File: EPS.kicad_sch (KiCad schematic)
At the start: 10 parts, among them J1 G125-MH10805M4-1AD1ADP, J2 PH1RA-02-UA, J3 WJ126V-5.0-2P, J4 10164359-00011LF

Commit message: Test commit
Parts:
- added J5: TC2050-IDC, TC2050-IDC, symbol HEDGE2:TC2050-IDC
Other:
- added sheet Power Conversion (powerConversion.kicad_sch)
- moved on the sheet: MH1, MH2, MH3, MH4

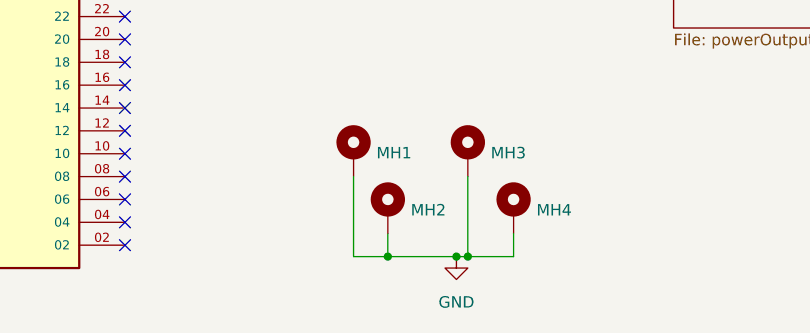
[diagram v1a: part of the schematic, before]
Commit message: updated battery sheet passives values
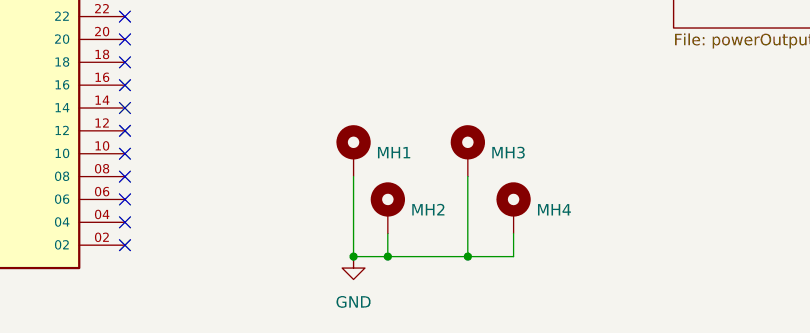
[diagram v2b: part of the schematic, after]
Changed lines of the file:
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@@
 	)
 	(junction
-		(at 104.14 179.07)
+		(at 105.41 179.07)
 		(diameter 0)
 		(color 0 0 0 0)
 	)
 	(junction
-		(at 105.41 179.07)
+		(at 92.71 179.07)
 		(diameter 0)
 		(color 0 0 0 0)
@@
 	(wire
 		(pts
-			(xy 96.52 179.07) (xy 104.14 179.07)
+			(xy 96.52 179.07) (xy 105.41 179.07)
 		)
 		(stroke
@@
 	(wire
 		(pts
-			(xy 105.41 179.07) (xy 104.14 179.07)
-		)
-		(stroke
-			(width 0)
-			(type default)
-		)
-	)
-	(wire
-		(pts
 			(xy 96.52 176.53) (xy 96.52 179.07)
 		)
@@
 	(symbol
 		(lib_id "power:GND")
-		(at 104.14 179.07 0)
+		(at 92.71 179.07 0)
 		(unit 1)
 		(exclude_from_sim no)
@@
 		(fields_autoplaced yes)
 		(property "Reference" "#PWR0105"
-			(at 104.14 185.42 0)
+			(at 92.71 185.42 0)
 			(effects
 				(font
@@
 		)
 		(property "Value" "GND"
-			(at 104.14 184.15 0)
+			(at 92.71 184.15 0)
 			(effects
 				(font
@@
 		)
 		(property "Footprint" ""
-			(at 104.14 179.07 0)
+			(at 92.71 179.07 0)
 			(effects
 				(font
@@
 		)
 		(property "Datasheet" ""
-			(at 104.14 179.07 0)
+			(at 92.71 179.07 0)
 			(effects
 				(font
@@
 		)
 		(property "Description" "Power symbol creates a global label with name \"GND\" , ground"
-			(at 104.14 179.07 0)
+			(at 92.71 179.07 0)
 			(effects
 				(font

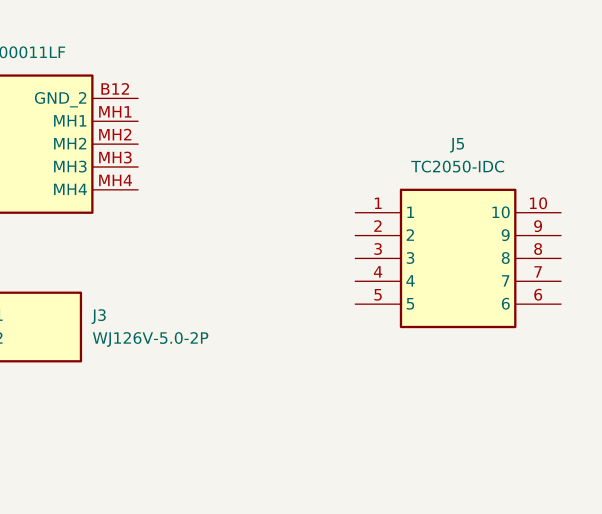
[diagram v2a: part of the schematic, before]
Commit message: Added CAN controller, got rid of one RS485 transceiver
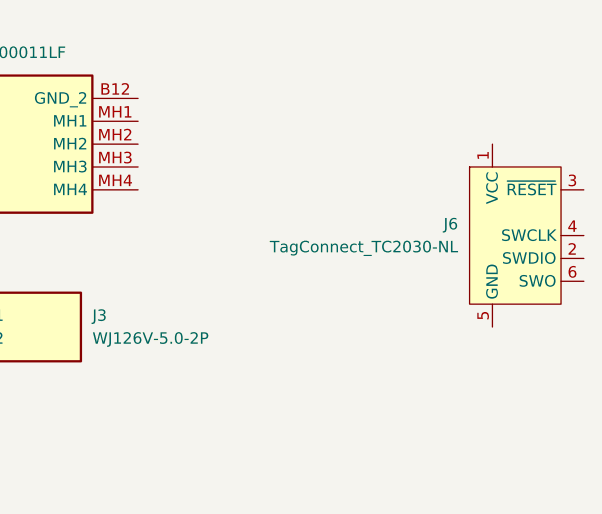
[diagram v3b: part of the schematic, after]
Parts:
- removed J5: TC2050-IDC, TC2050-IDC, symbol HEDGE2:TC2050-IDC
- added J6: TagConnect_TC2030-NL, Connector:Tag-Connect_TC2030-IDC-NL_2x03_P1.27mm_Vertical, symbol Connector:Conn_ARM_SWD_TagConnect_TC2030-NL
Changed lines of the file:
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@@
-	)
-	(symbol
-		(lib_id "HEDGE2:TC2050-IDC")
-		(at 247.65 40.64 0)
-		(unit 1)
-		(exclude_from_sim no)
-		(in_bom yes)
-		(on_board yes)
-		(dnp no)
-		(fields_autoplaced yes)
-		(property "Reference" "J5"
-			(at 259.08 33.02 0)
-			(effects
-				(font
-					(size 1.27 1.27)
-				)
-			)
-		)
-		(property "Value" "TC2050-IDC"
-			(at 259.08 35.56 0)
-			(effects
-				(font
-					(size 1.27 1.27)
-				)
-			)
-		)
-		(property "Footprint" "TC2050-IDC"
-			(at 266.7 135.56 0)
-			(effects
-				(font
-					(size 1.27 1.27)
-				)
-				(justify left top)
-				(hide yes)
-			)
-		)
-		(property "Datasheet" "https://datasheet.datasheetarchive.com/originals/distributors/Datasheets_SAMA/51f607a36a24a0aceedaa5d6ebc30014.pdf"
-			(at 266.7 235.56 0)
-			(effects
-				(font
-					(size 1.27 1.27)
-				)
-				(justify left top)
-				(hide yes)
-			)
-		)
-		(property "Description" "Plug of nails cable"
-			(at 247.65 40.64 0)
-			(effects
-				(font
-					(size 1.27 1.27)
-				)
-				(hide yes)
-			)
-		)
-		(property "Height" ""
-			(at 266.7 435.56 0)
-			(effects
-				(font
-					(size 1.27 1.27)
-				)
-				(justify left top)
-				(hide yes)
-			)
-		)
-		(property "Manufacturer_Name" "Tag Connect"
-			(at 266.7 535.56 0)
-			(effects
-				(font
-					(size 1.27 1.27)
-				)
-				(justify left top)
-				(hide yes)
-			)
-		)
-		(property "Manufacturer_Part_Number" "TC2050-IDC"
-			(at 266.7 635.56 0)
-			(effects
-				(font
-					(size 1.27 1.27)
-				)
-				(justify left top)
-				(hide yes)
-			)
-		)
-		(property "Mouser Part Number" ""
-			(at 266.7 735.56 0)
-			(effects
-				(font
-					(size 1.27 1.27)
-				)
-				(justify left top)
-				(hide yes)
-			)
-		)
-		(property "Mouser Price/Stock" ""
-			(at 266.7 835.56 0)
-			(effects
-				(font
-					(size 1.27 1.27)
-				)
-				(justify left top)
-				(hide yes)
-			)
-		)
-		(property "Arrow Part Number" ""
-			(at 266.7 935.56 0)
-			(effects
-				(font
-					(size 1.27 1.27)
-				)
-				(justify left top)
-				(hide yes)
-			)
-		)
-		(property "Arrow Price/Stock" ""
-			(at 266.7 1035.56 0)
-			(effects
-				(font
-					(size 1.27 1.27)
-				)
-				(justify left top)
-				(hide yes)
-			)
-		)
-		(pin "9"
-		)
-		(pin "6"
-		)
-		(pin "1"
-		)
-		(pin "5"
-		)
-		(pin "4"
-		)
-		(pin "2"
-		)
-		(pin "3"
-		)
-		(pin "8"
-		)
-		(pin "7"
-		)
-		(pin "10"
-		)
-		(instances
-			(project "EPS"
-				(path "/7b605902-d0e0-4baa-b797-611cfe27637f"
-					(reference "J5")
-					(unit 1)
-				)
-			)
-		)
 	)
 	(symbol
@@
 					(unit 1)
 				)
+			)
+		)
+	)
+	(symbol
+		(lib_id "Connector:Conn_ARM_SWD_TagConnect_TC2030-NL")
+		(at 265.43 43.18 0)
+		(unit 1)
+		(exclude_from_sim no)
+		(in_bom no)
+		(on_board yes)
+		(dnp no)
+		(fields_autoplaced yes)
+		(property "Reference" "J6"
+			(at 259.08 41.9099 0)
+			(effects
+				(font
+					(size 1.27 1.27)
+				)
+				(justify right)
+			)
+		)
+		(property "Value" "TagConnect_TC2030-NL"
+			(at 259.08 44.4499 0)
+			(effects
+				(font
+					(size 1.27 1.27)
+				)
+				(justify right)
+			)
+		)
+		(property "Footprint" "Connector:Tag-Connect_TC2030-IDC-NL_2x03_P1.27mm_Vertical"
+			(at 265.43 60.96 0)
+			(effects
+				(font
+					(size 1.27 1.27)
+				)
+				(hide yes)
+			)
+		)
+		(property "Datasheet" "https://www.tag-connect.com/wp-content/uploads/bsk-pdf-manager/TC2030-CTX_1.pdf"
+			(at 265.43 58.42 0)
+			(effects
+				(font
+					(size 1.27 1.27)
+				)
+				(hide yes)
+			)
+		)
+		(property "Description" "Tag-Connect ARM Cortex SWD JTAG connector, 6 pin, no legs"
+			(at 265.43 43.18 0)
+			(effects
+				(font
+					(size 1.27 1.27)
+				)
+				(hide yes)
+			)
+		)
+		(pin "6"
+		)
+		(pin "1"
+		)
+		(pin "5"
+		)
+		(pin "3"
+		)
+		(pin "4"
+		)
+		(pin "2"
+		)
+		(instances
+			(project ""
+				(path "/7b605902-d0e0-4baa-b797-611cfe27637f"
+					(reference "J6")
+					(unit 1)
+				)

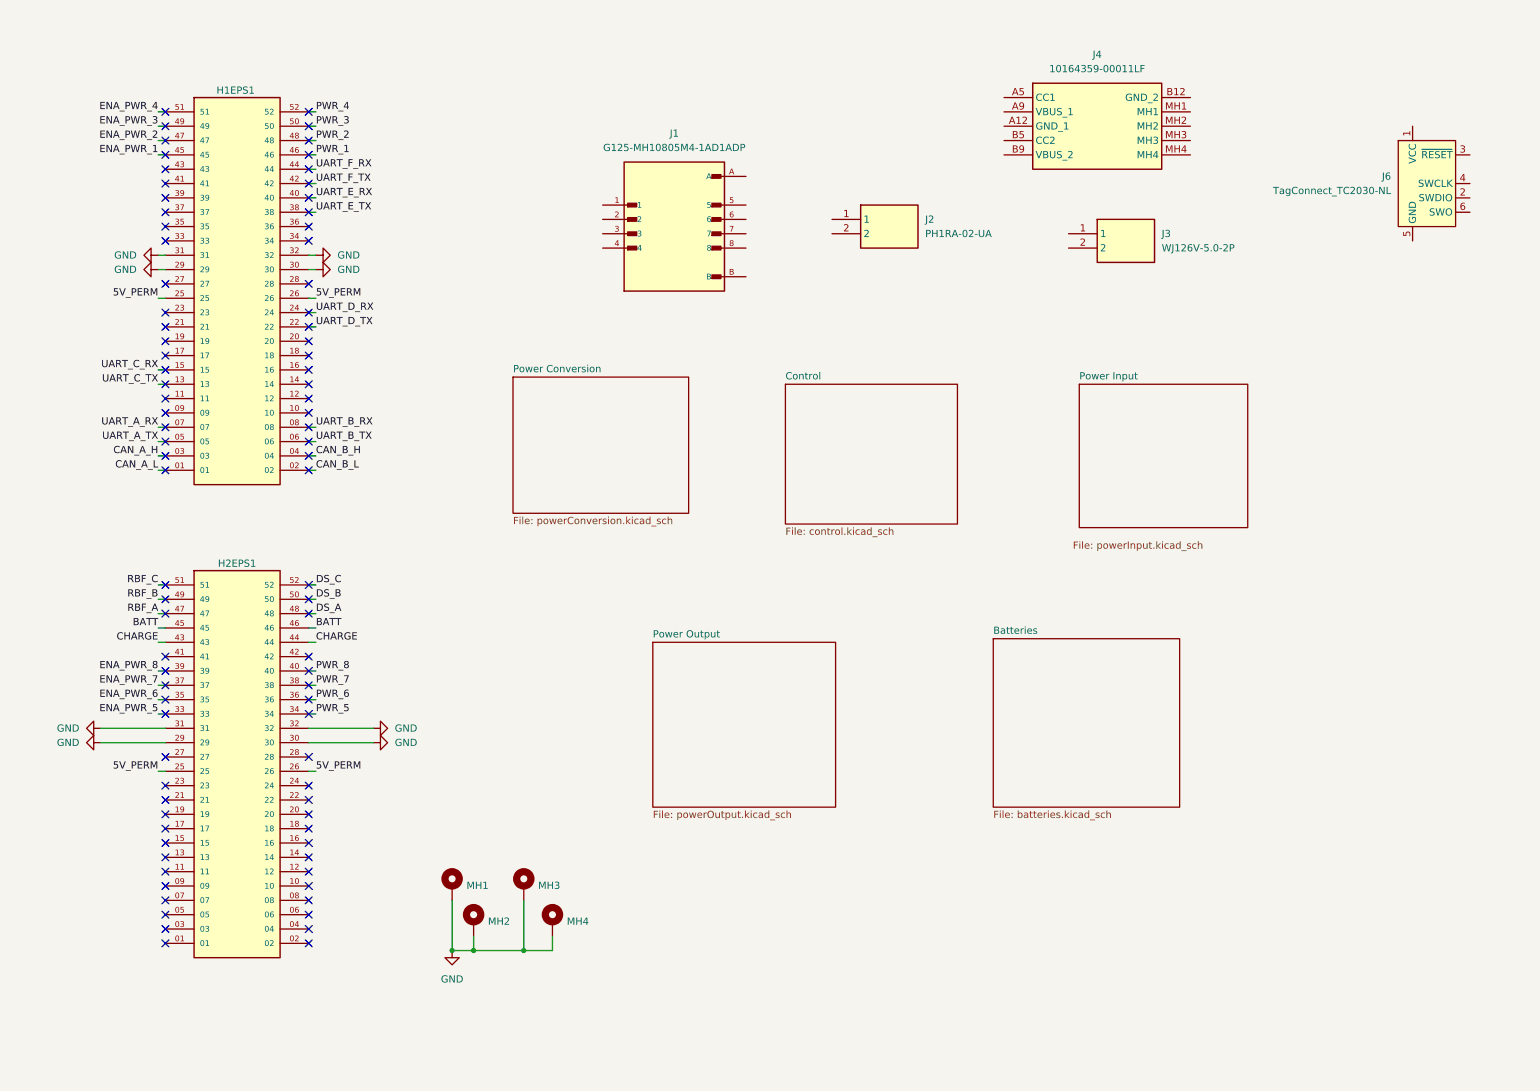
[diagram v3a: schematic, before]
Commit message: updates to connectors
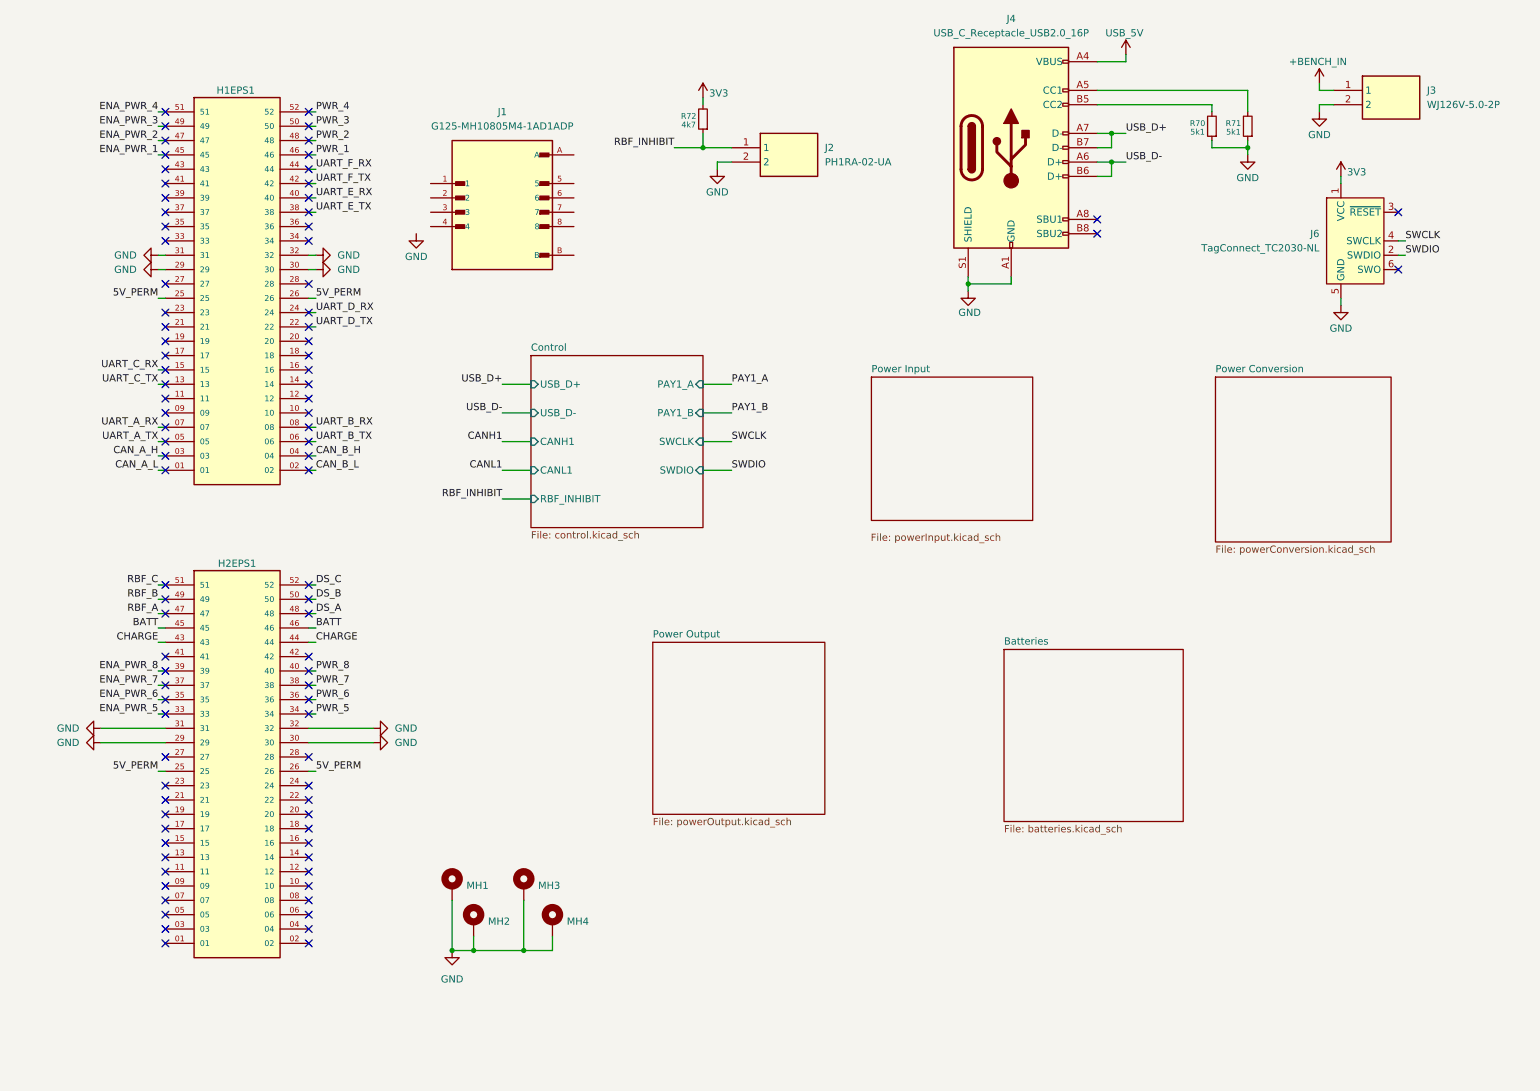
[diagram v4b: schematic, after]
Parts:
- removed J4: 10164359-00011LF, 1016435900011LF, symbol HEDGE2:10164359-00011LF
- added J4: USB_C_Receptacle_USB2.0_16P, symbol Connector:USB_C_Receptacle_USB2.0_16P
- added R70, R71: 5k1, symbol Device:R_Small
- added R72: 4k7, symbol Device:R_Small
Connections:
- net GND: now also J2.2, J3.2, J6.5 (GND), J4.A1 (GND), J4.A12 (GND), J4.B1 (GND), J4.B12 (GND), J4.S1 (SHIELD), R70.1, R71.1
- net +BENCH_IN: now reaches J3.1
- net RBF_INHIBIT: now reaches J2.1
- net RBF_INHIBIT: now also R72.1
- net 3V3: now reaches J6.1 (VCC)
- net 3V3: now also R72.2
- net SWDIO: now reaches J6.2 (SWDIO)
- net SWCLK: now reaches J6.4 (SWCLK)
- new net: J4.B5 (CC2), R70.2
- new net: J4.A5 (CC1), R71.2
- new net USB_5V: J4.A4 (VBUS), J4.A9 (VBUS), J4.B4 (VBUS), J4.B9 (VBUS)
- new net USB_D+: J4.A7 (D-), J4.B7 (D-)
- new net USB_D-: J4.A6 (D+), J4.B6 (D+)
- no-connect marks 88 -> 92
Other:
- sheet Control ports: added CANH1, CANL1, PAY1_A, PAY1_B, RBF_INHIBIT, SWCLK, SWDIO, USB_D+, USB_D-; removed none
- moved on the sheet: J1, J2, J3, J6
